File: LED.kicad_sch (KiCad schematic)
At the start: 60 parts

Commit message: stuff?
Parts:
- added D62, D63, D64, D65, D66, D67, D68, D69, D70, D71, D72, D73, D74, D75: LED_Small, symbol Device:LED_Small
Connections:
- net M1: now also D62.1 (K)
- net M2: now also D64.1 (K); no longer D18.1 (K), D20.1 (K), D31.2 (A), D33.2 (A), D34.1 (K), D35.2 (A), D37.2 (A), D39.2 (A), D4.1 (K), D41.2 (A), D43.2 (A), D45.2 (A), D47.2 (A), D48.1 (K), D49.2 (A), D51.2 (A), D53.2 (A), D55.2 (A), D57.2 (A), D6.1 (K)
- net M5: now also D63.2 (A), D65.2 (A), D67.2 (A), D69.2 (A), D71.2 (A), D73.2 (A), D75.2 (A)
- net M6: now also D70.1 (K)
- net M7: now also D72.1 (K)
- net M8: now also D74.1 (K)
- net COLLON renamed COLON
- new net: D68.2 (A), D69.1 (K)
- new net: D66.2 (A), D67.1 (K)
- new net: D72.2 (A), D73.1 (K)
- new net: D62.2 (A), D63.1 (K)
- new net: D64.2 (A), D65.1 (K)
- new net: D70.2 (A), D71.1 (K)
- new net: D74.2 (A), D75.1 (K)
- new net M3: D18.1 (K), D31.2 (A), D33.2 (A), D35.2 (A), D37.2 (A), D39.2 (A), D4.1 (K), D41.2 (A), D43.2 (A), D48.1 (K), D66.1 (K)
- new net M4: D20.1 (K), D34.1 (K), D45.2 (A), D47.2 (A), D49.2 (A), D51.2 (A), D53.2 (A), D55.2 (A), D57.2 (A), D6.1 (K), D68.1 (K)
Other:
- note added: "COLON"
- note added: "DAYS"
- note added: "HOURS"
- note added: "MINUTES"
- moved on the sheet: D58, D59, D60, D61

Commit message: new resistors for LED matrix
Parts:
- added R16, R17, R18, R19, R20, R21, R22, R23, R24, R25, R26, R27, R28: 50R, symbol Device:R
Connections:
- net M1: now also R16.1, R24.1; no longer D11.2 (A), D13.2 (A), D15.2 (A), D16.1 (K), D3.2 (A), D30.1 (K), D44.1 (K), D5.2 (A), D62.1 (K), D7.2 (A), D9.2 (A)
- net M2: now also R17.1, R25.1; no longer D17.2 (A), D19.2 (A), D2.1 (K), D21.2 (A), D23.2 (A), D25.2 (A), D27.2 (A), D29.2 (A), D32.1 (K), D46.1 (K), D64.1 (K)
- net M3: now also R18.1, R26.1; no longer D18.1 (K), D31.2 (A), D33.2 (A), D35.2 (A), D37.2 (A), D39.2 (A), D4.1 (K), D41.2 (A), D43.2 (A), D48.1 (K), D66.1 (K)
- net M4: now also R19.1, R27.1; no longer D20.1 (K), D34.1 (K), D45.2 (A), D47.2 (A), D49.2 (A), D51.2 (A), D53.2 (A), D55.2 (A), D57.2 (A), D6.1 (K), D68.1 (K)
- net M5: now also R20.1, R28.1; no longer D22.1 (K), D36.1 (K), D50.1 (K), D63.2 (A), D65.2 (A), D67.2 (A), D69.2 (A), D71.2 (A), D73.2 (A), D75.2 (A), D8.1 (K)
- net M6: now also R21.1; no longer D10.1 (K), D24.1 (K), D38.1 (K), D52.1 (K), D70.1 (K)
- net M7: now also R22.1; no longer D12.1 (K), D26.1 (K), D40.1 (K), D54.1 (K), D72.1 (K)
- net M8: now also R23.1; no longer D14.1 (K), D28.1 (K), D42.1 (K), D56.1 (K), D74.1 (K)
- new net: D20.1 (K), D34.1 (K), D6.1 (K), D68.1 (K), R19.2
- new net: D12.1 (K), D26.1 (K), D40.1 (K), D54.1 (K), D72.1 (K), R22.2
- new net: D17.2 (A), D19.2 (A), D21.2 (A), D23.2 (A), D25.2 (A), D27.2 (A), D29.2 (A), R25.2
- new net: D11.2 (A), D13.2 (A), D15.2 (A), D3.2 (A), D5.2 (A), D7.2 (A), D9.2 (A), R24.2
- new net: D63.2 (A), D65.2 (A), D67.2 (A), D69.2 (A), D71.2 (A), D73.2 (A), D75.2 (A), R28.2
- new net: D18.1 (K), D4.1 (K), D48.1 (K), D66.1 (K), R18.2
- new net: D31.2 (A), D33.2 (A), D35.2 (A), D37.2 (A), D39.2 (A), D41.2 (A), D43.2 (A), R26.2
- new net: D45.2 (A), D47.2 (A), D49.2 (A), D51.2 (A), D53.2 (A), D55.2 (A), D57.2 (A), R27.2
- new net: D14.1 (K), D28.1 (K), D42.1 (K), D56.1 (K), D74.1 (K), R23.2
- new net: D22.1 (K), D36.1 (K), D50.1 (K), D8.1 (K), R20.2
- new net: D16.1 (K), D30.1 (K), D44.1 (K), D62.1 (K), R16.2
- new net: D10.1 (K), D24.1 (K), D38.1 (K), D52.1 (K), D70.1 (K), R21.2
- new net: D2.1 (K), D32.1 (K), D46.1 (K), D64.1 (K), R17.2

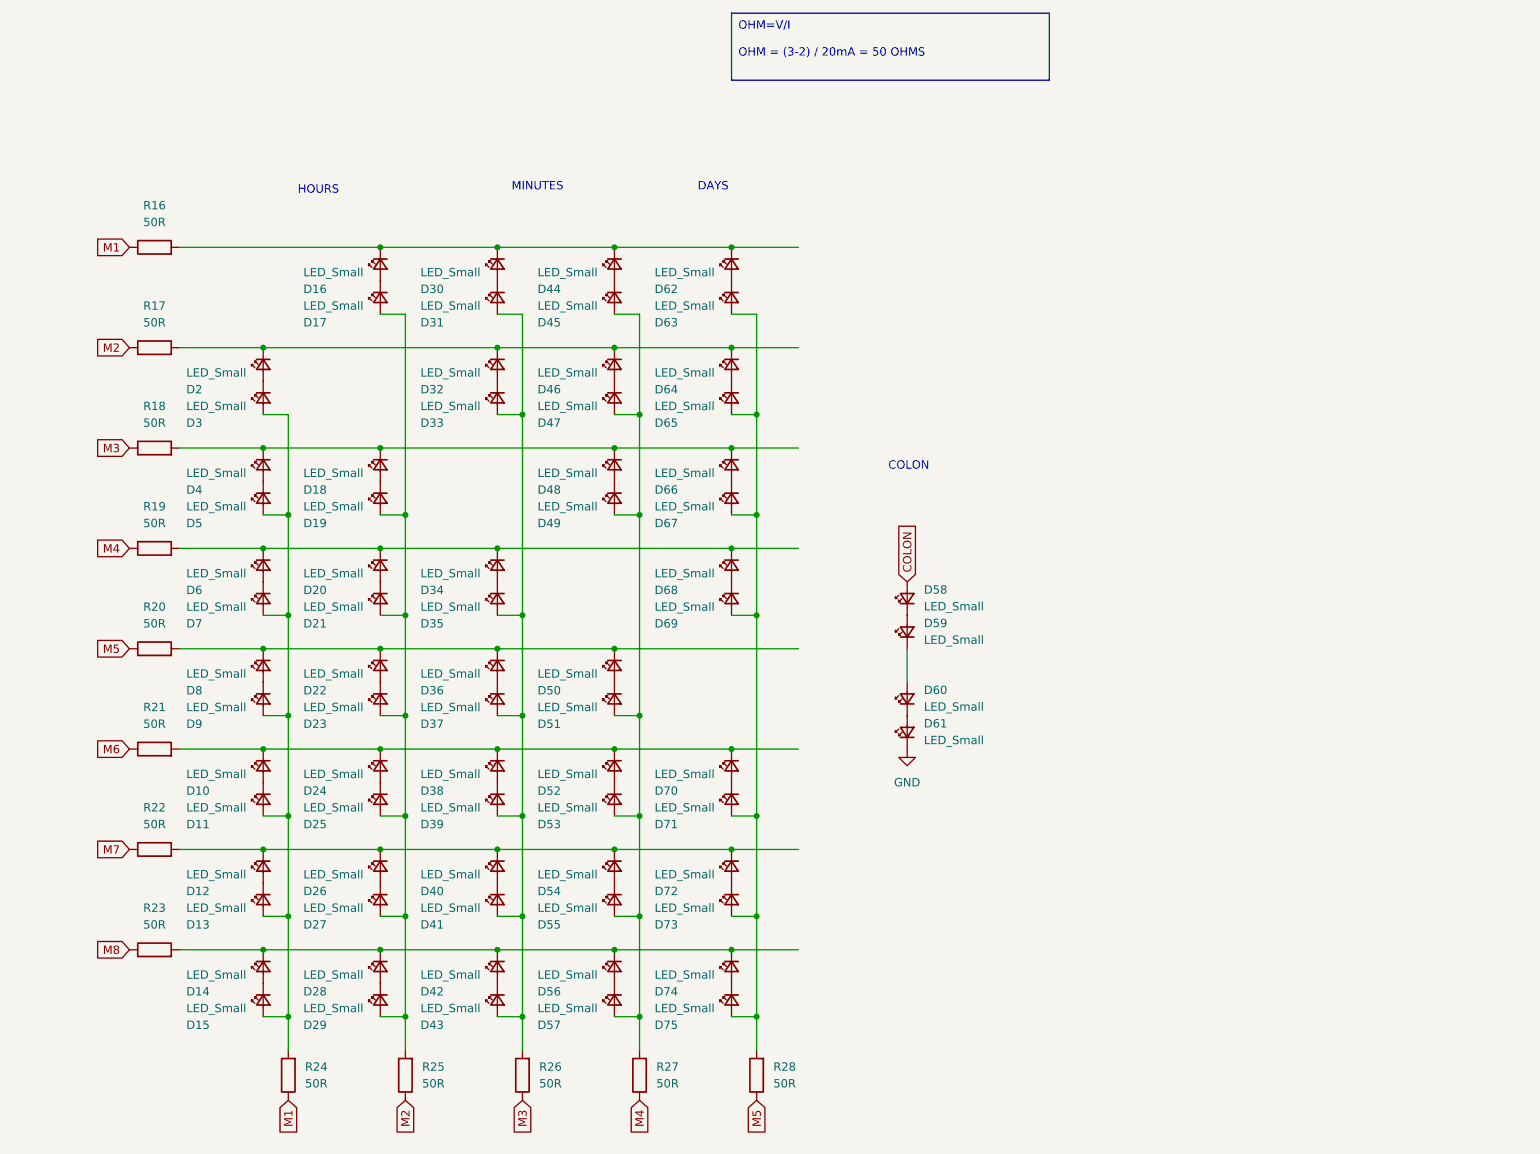
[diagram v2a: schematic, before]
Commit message: actually grounded STM, changed charlie plexed resistors, added note for charging logic, added switch for the 5V logic detection
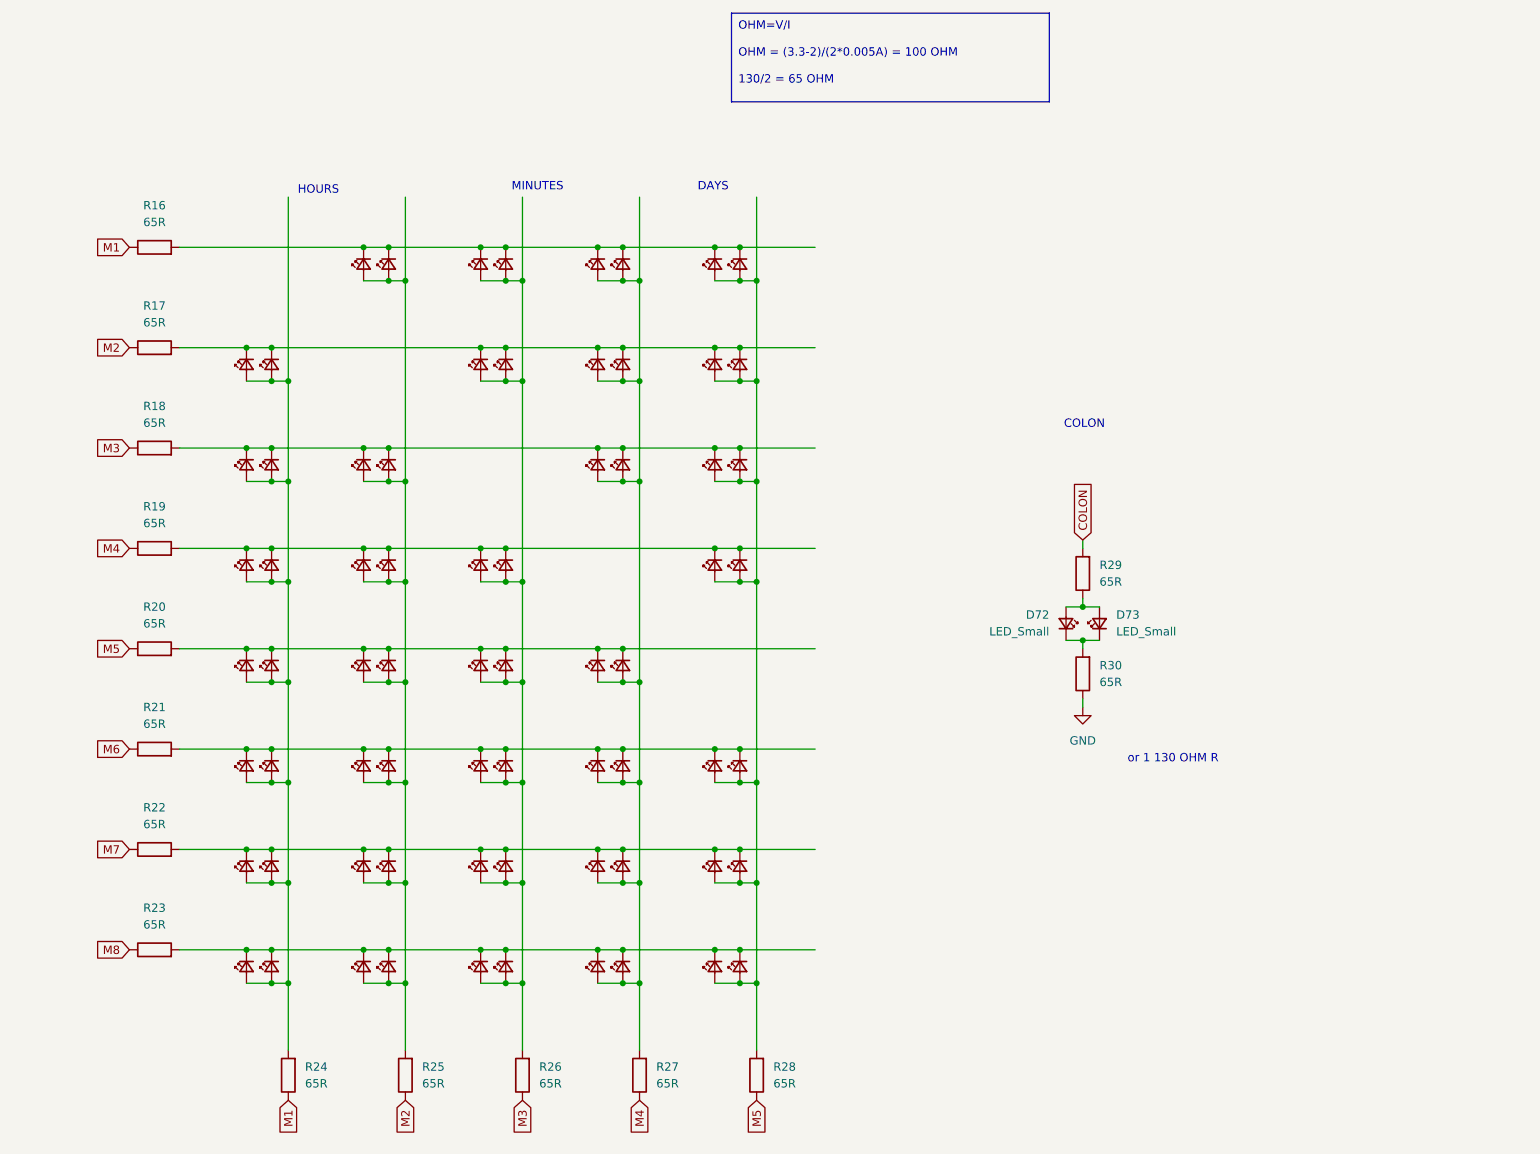
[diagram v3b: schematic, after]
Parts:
- removed D74, D75, D8: LED_Small, symbol Device:LED_Small
- added D14: LED_Small, symbol Device:LED_Small
- added R29, R30: 65R, symbol Device:R
- R16, R17, R18, R19, R20, R21, R22, R23, R24, R25, R26, R27, R28: value 50R -> 65R
- renumbered D14 to D8
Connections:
- net COLON: now also R29.2; no longer D58.2 (A)
- net GND: now also R30.1; no longer D61.1 (K)
- net at D20.1 (K), D34.1 (K), D6.1 (K): now also D13.1 (K), D27.1 (K), D41.1 (K), D48.1 (K), D55.1 (K), D62.1 (K), D69.1 (K), R21.2; no longer D68.1 (K), R19.2
- net at D21.1 (K): now also D28.1 (K), D35.1 (K), D42.1 (K), D49.1 (K), D56.1 (K), D63.1 (K), D7.1 (K), D70.1 (K), R22.2, D14.1 (K); no longer D20.2 (A)
- net at D12.1 (K), D26.1 (K), D40.1 (K)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: now also D19.1 (K), D33.1 (K), D47.1 (K), D5.1 (K), R20.2; no longer D72.1 (K), R22.2
- net at D26.2 (A): now also D16.2 (A), D17.2 (A), D18.2 (A), D19.2 (A), D20.2 (A), D21.2 (A), D22.2 (A), D23.2 (A), D24.2 (A), D25.2 (A), D27.2 (A), D28.2 (A), D29.2 (A), R25.2; no longer D27.1 (K)
- net at D25.1 (K): now also D11.1 (K), D18.1 (K), D32.1 (K), D39.1 (K), D4.1 (K), D61.1 (K), D68.1 (K), R19.2; no longer D24.2 (A)
- net at D4.2 (A): now also D10.2 (A), D11.2 (A), D12.2 (A), D13.2 (A), D15.2 (A), D2.2 (A), D3.2 (A), D5.2 (A), D6.2 (A), D7.2 (A), D8.2 (A), D9.2 (A), R24.2, D14.2 (A); no longer D5.1 (K)
- net at D68.2 (A): now also D58.2 (A), D59.2 (A), D60.2 (A), D61.2 (A), D62.2 (A), D63.2 (A), D64.2 (A), D65.2 (A), D66.2 (A), D67.2 (A), D69.2 (A), D70.2 (A), D71.2 (A), R28.2; no longer D69.1 (K)
- net at D40.2 (A): now also D30.2 (A), D31.2 (A), D32.2 (A), D33.2 (A), D34.2 (A), D35.2 (A), D36.2 (A), D37.2 (A), D38.2 (A), D39.2 (A), D41.2 (A), D42.2 (A), D43.2 (A), R26.2; no longer D41.1 (K)
- net at D67.1 (K): now also D10.1 (K), D17.1 (K), D24.1 (K), D3.1 (K), D46.1 (K), D53.1 (K), D60.1 (K), R18.2; no longer D66.2 (A)
- net at D43.1 (K): now also D15.1 (K), D22.1 (K), D29.1 (K), D36.1 (K), D50.1 (K), D57.1 (K), D64.1 (K), D71.1 (K), D8.1 (K), R23.2; no longer D42.2 (A)
- net at D52.2 (A): now also D44.2 (A), D45.2 (A), D46.2 (A), D47.2 (A), D48.2 (A), D49.2 (A), D50.2 (A), D51.2 (A), D53.2 (A), D54.2 (A), D55.2 (A), D56.2 (A), D57.2 (A), R27.2; no longer D53.1 (K)
- net at D73.1 (K): now also D72.1 (K), R30.2; no longer D72.2 (A)
- net at D45.1 (K): now also D2.1 (K), D31.1 (K), D38.1 (K), D52.1 (K), D59.1 (K), D66.1 (K), D9.1 (K), R17.2; no longer D44.2 (A)
- net at D51.1 (K): now also D16.1 (K), D23.1 (K), D30.1 (K), D37.1 (K), D44.1 (K), D58.1 (K), D65.1 (K), R16.2; no longer D50.2 (A)
- new net: D72.2 (A), D73.2 (A), R29.1
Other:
- note added: "or 1 130 OHM R"

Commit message: done loads, added indication LED, changed how switches works, added footprints for lots of things, set up editor for laying things out
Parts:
- D10, D11, D12, D13, D14, D15, D16, D17, D18, D19, D2, D20, D21, D22, D23, D24, D25, D26, D27, D28, D29, D3, D30, D31, D32, D33, D34, D35, D36, D37, D38, D39, D4, D40, D41, D42, D43, D44, D45, D46, D47, D48, D49, D5, D50, D51, D52, D53, D54, D55, D56, D57, D58, D59, D6, D60, D61, D62, D63, D64, D65, D66, D67, D68, D69, D7, D70, D71, D72, D73, D8, D9: footprint (none) -> LED_SMD:LED_0603_1608Metric_Pad1.05x0.95mm_HandSolder
- R16, R17, R18, R19, R20, R21, R22, R23, R24, R25, R26, R27, R28, R29, R30: value 65R -> 68R; footprint (none) -> Resistor_SMD:R_0402_1005Metric_Pad0.72x0.64mm_HandSolder

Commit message: layed out the LED display
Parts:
- D10, D11, D12, D13, D14, D15, D16, D17, D18, D19, D2, D20, D21, D22, D23, D24, D25, D26, D27, D28, D29, D3, D30, D31, D32, D33, D34, D35, D36, D37, D38, D39, D4, D40, D41, D42, D43, D44, D45, D46, D47, D48, D49, D5, D50, D51, D52, D53, D54, D55, D56, D57, D58, D59, D6, D60, D61, D62, D63, D64, D65, D66, D67, D68, D69, D7, D70, D71, D72, D73, D8, D9: footprint LED_SMD:LED_0603_1608Metric_Pad1.05x0.95mm_HandSolder -> LED_SMD:LED_0402_1005Metric_Pad0.77x0.64mm_HandSolder
